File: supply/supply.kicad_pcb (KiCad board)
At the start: 2 copper layers, 45 parts, among them U1 ALTAIR04-900, U2 AP1117-50, U3 MCP73811T-420I-OT, U4 AP9101CK

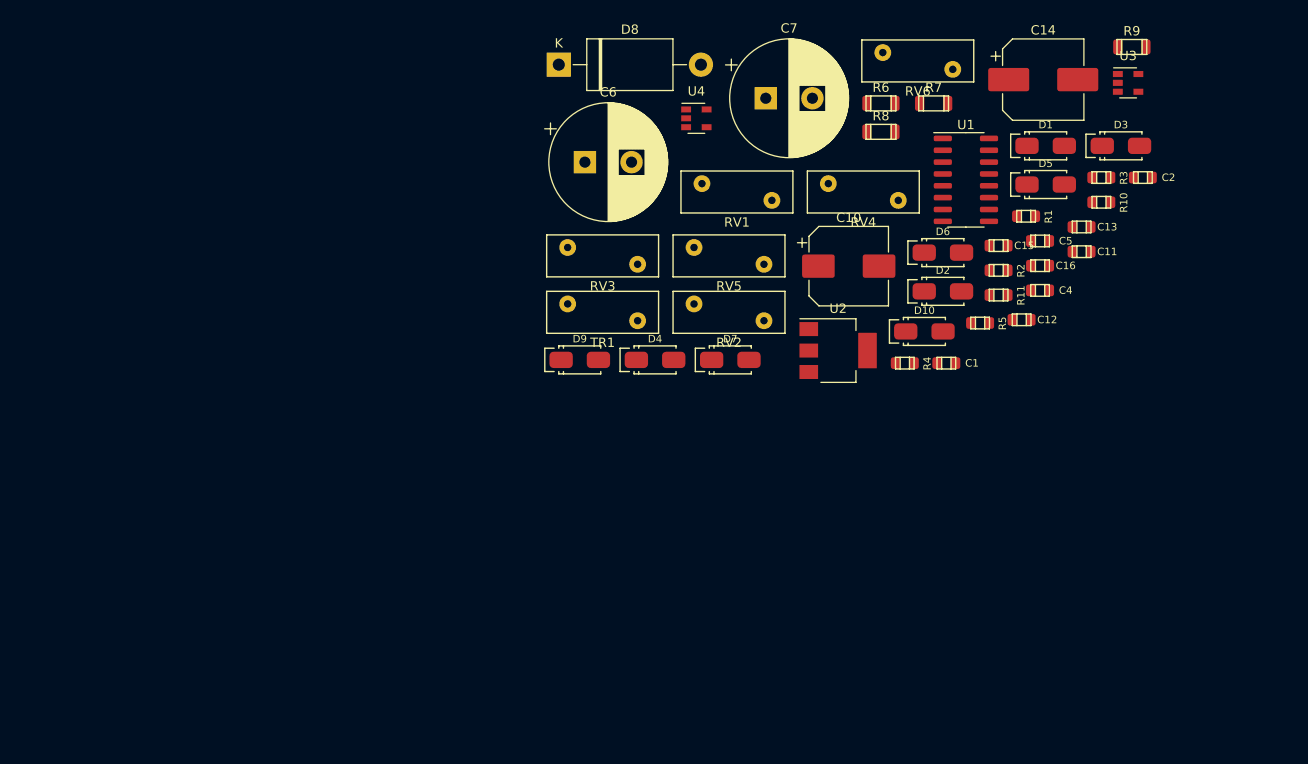
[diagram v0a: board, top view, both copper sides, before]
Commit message: add xfmr footprint
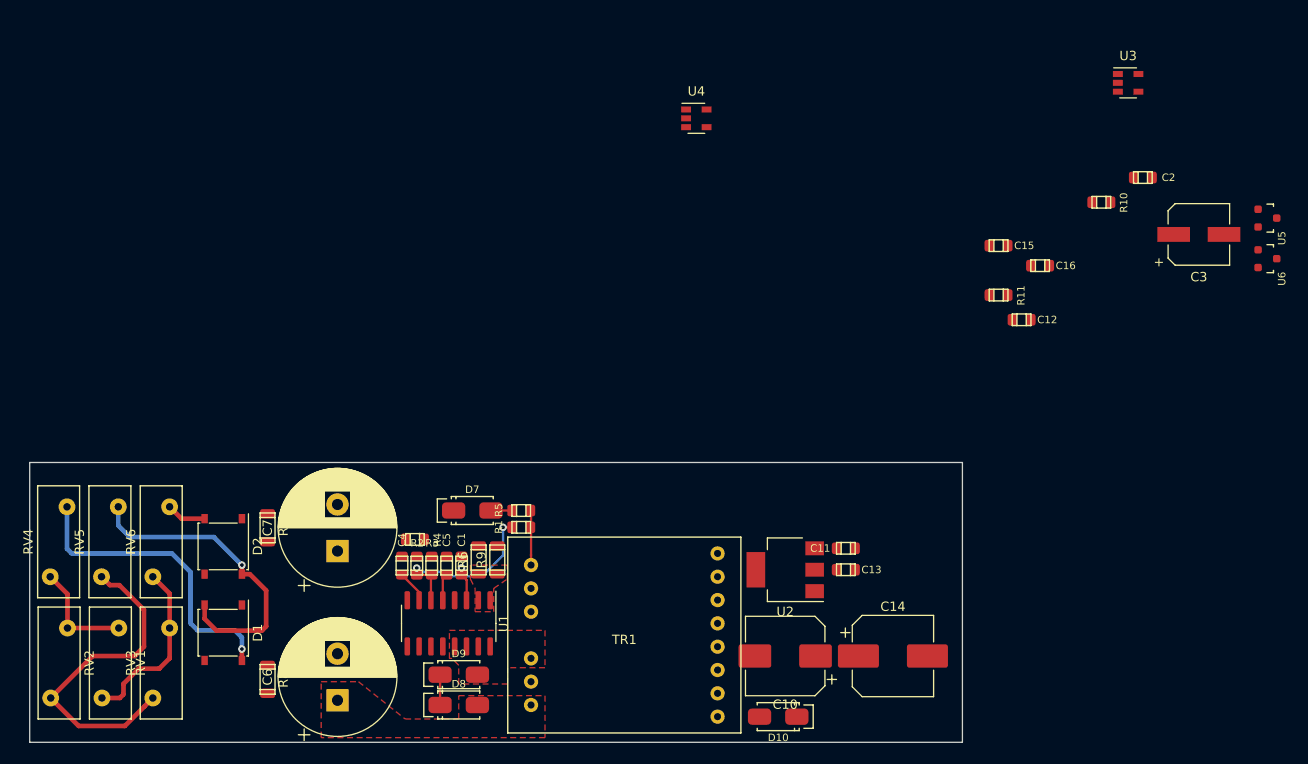
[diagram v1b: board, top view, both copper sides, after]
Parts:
- removed D3, D4, D5, D6: D, stmbl:SMA_Standard
- added C3: 2.2µ, Capacitors_SMD:CP_Elec_6.3x4.5, F.Cu at (165.3, 95.5)
- added U5: NFET, stmbl:SOT-23, F.Cu at (172.7, 93.8)
- added U6: NFET, stmbl:SOT-23, F.Cu at (172.7, 98.2)
- D1, D2: value D -> D_Bridge_+A-A; footprint stmbl:SMA_Standard -> Diodes_SMD:Diode_Bridge_MBLS
- D8: footprint Diode_THT:D_DO-201AE_P15.24mm_Horizontal -> stmbl:SMA_Standard
- TR1: footprint Varistor:RV_Disc_D12mm_W4.5mm_P7.5mm -> altair04:750871110
- moved D1 102.5 mm to (60.8, 138.2), turned to 270 degrees
- moved RV6 90.7 mm to (55.0, 124.8), turned to 270 degrees
- moved RV4 88.7 mm to (44.0, 124.8), turned to 270 degrees
- moved R8 88.2 mm to (65.5, 143.2), turned to 270 degrees
- moved R9 87.5 mm to (90.1, 130.4), turned to 90 degrees
- moved RV1 84.7 mm to (47.8, 145.2), turned to 90 degrees
- moved R7 84.7 mm to (65.5, 127.0), turned to 270 degrees
- moved R3 83.0 mm to (83.1, 131.1), turned to 90 degrees
- moved D2 81.9 mm to (60.8, 129.0), turned to 270 degrees
- moved RV2 80.9 mm to (42.2, 145.2), turned to 90 degrees
- moved C4 74.5 mm to (79.9, 131.1), turned to 90 degrees
- moved U1 73.0 mm to (84.9, 137.2), turned to 270 degrees
- moved C5 72.5 mm to (84.7, 131.1), turned to 90 degrees
- moved R2 69.9 mm to (81.5, 131.1), turned to 90 degrees
- moved D8 69.5 mm to (86.0, 146.0)
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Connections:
- net Net-(C?1556916859-Pad1) renamed /COMP
- net Net-(C?1556919213-Pad1) renamed /IREF
- net Net-(C?1556958770-Pad1) renamed /VCC
- net Net-(R?1556909002-Pad1) renamed /SRC
- net Net-(R?1556926018-Pad1) renamed /FB
- D10 pad 2: Net-(D?1556809417-Pad2) -> Net-(D10-Pad2)
- D2 pad 1: Net-(D1-Pad2) -> DC+
- D2 pad 2: GND -> Net-(D2-Pad2)
- D9 pad 2: Net-(D?1556997350-Pad2) -> /DRN
- R1 pad 1: Net-(R?1556927718-Pad1) -> Net-(R1-Pad1)
- R5 pad 1: Net-(R?1556927718-Pad1) -> Net-(R1-Pad1)
- RV4 pad 1: Net-(D1-Pad2) -> Net-(D1-Pad4)
- RV5 pad 1: Net-(D?1556584705-Pad2) -> Net-(D1-Pad2)
- RV6 pad 1: Net-(D?1556585160-Pad2) -> Net-(D2-Pad2)
- TR1 pad 1: GND -> Net-(R1-Pad1)
- U1 pad 13: Net-(D?1556997350-Pad2) -> /DRN
- U1 pad 14: Net-(D?1556997350-Pad2) -> /DRN
- U1 pad 15: Net-(D?1556997350-Pad2) -> /DRN
- U1 pad 16: Net-(D?1556997350-Pad2) -> /DRN
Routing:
- net L2: track 0.00 -> 35.7 mm
- net Net-(D1-Pad2): track 0.00 -> 33.9 mm, vias 0 -> 1
- net Net-(D1-Pad4): track 0.00 -> 32.9 mm, vias 0 -> 1
- net /FB: track 0.00 -> 19.6 mm, vias 0 -> 2
- net L3: track 0.00 -> 19.2 mm
- net L1: track 0.00 -> 11.8 mm
- net Net-(R1-Pad1): track 0.00 -> 5.60 mm
- net Net-(D2-Pad2): track 0.00 -> 4.28 mm
- net /VCC: track 0.00 -> 3.71 mm, vias 0 -> 1
- net /COMP: track 0.00 -> 3.48 mm
- net Net-(D8-Pad1): track 0.00 -> 3.25 mm
- net /IREF: track 0.00 -> 2.89 mm
- net Net-(D7-Pad2): track 0.00 -> 2.25 mm
- added copper zone on F.Cu, net /DRN
- added copper zone on F.Cu, net /SRC
- added copper zone on F.Cu, net DC+
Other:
- board outline added: 100 x 30 mm
- net class power added: clearance 2, trace_width 0.5, via_dia 0.8, via_drill 0.4
